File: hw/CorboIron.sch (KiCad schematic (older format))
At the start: 82 parts, among them P1 CONN_01X03, P10 CONN_01X04, P11 CONN_01X04, P2 CONN_01X03, P3 CONN_01X03, P4 DIL32, P5 CONN_01X03, P6 CONN_01X04, P7 CONN_01X02, P8 CONN_01X03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

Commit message: Started PCB
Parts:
- C1, C10, C2, C3, C4, C5, C6, C7: footprint (none) -> Discret:CV3-30PF
- C8, C9: footprint (none) -> Capacitors_SMD:C_1206_HandSoldering
- D1, D3, D4, D5, D7, D9: footprint (none) -> Diodes_SMD:DO-214BA
- D10, D2, D6, D8: footprint (none) -> LEDs:LED_1206
- JP1, JP2: footprint (none) -> Pin_Headers:Pin_Header_Straight_1x02
- P1, P2, P3, P5: footprint (none) -> Connect:bornier3
- P10, P11, P6: footprint (none) -> Pin_Headers:Pin_Header_Straight_1x04
- P4: footprint (none) -> Housings_DIP:DIP-32_W15.24mm_LongPads
- P7: footprint (none) -> Connect:bornier2
- P8, P9: footprint (none) -> Pin_Headers:Pin_Header_Straight_1x03
- Q1, Q2, Q3, Q4: footprint DPAK-5 -> SMD_Packages:DPAK5
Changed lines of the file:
@@
 LIBS:contrib
 LIBS:valves
+LIBS:CorboIron-cache
 EELAYER 25 0
 EELAYER END
@@
 F 0 "P4" H 1650 7750 50  0000 C CNN
 F 1 "DIL32" V 1650 6800 50  0000 C CNN
-F 2 "" H 1650 6800 50  0001 C CNN
+F 2 "Housings_DIP:DIP-32_W15.24mm_LongPads" H 1650 6800 50  0001 C CNN
 F 3 "" H 1650 6800 50  0000 C CNN
 	1    1650 6800
@@
 F 0 "C2" H 1925 3850 50  0000 L CNN
 F 1 "CP1" H 1925 3650 50  0000 L CNN
-F 2 "" H 1900 3750 50  0001 C CNN
+F 2 "Discret:CV3-30PF" H 1900 3750 50  0001 C CNN
 F 3 "" H 1900 3750 50  0000 C CNN
 	1    1900 3750
@@
 F 0 "D3" H 2400 3850 50  0000 C CNN
 F 1 "D" H 2400 3650 50  0000 C CNN
-F 2 "" H 2400 3750 50  0001 C CNN
+F 2 "Diodes_SMD:DO-214BA" H 2400 3750 50  0001 C CNN
 F 3 "" H 2400 3750 50  0000 C CNN
 	1    2400 3750
@@
 F 0 "D4" H 2150 4000 50  0000 C CNN
 F 1 "D" H 2150 3800 50  0000 C CNN
-F 2 "" H 2150 3900 50  0001 C CNN
+F 2 "Diodes_SMD:DO-214BA" H 2150 3900 50  0001 C CNN
 F 3 "" H 2150 3900 50  0000 C CNN
 	1    2150 3900
@@
 F 0 "C3" H 2675 4000 50  0000 L CNN
 F 1 "CP1" H 2675 3800 50  0000 L CNN
-F 2 "" H 2650 3900 50  0001 C CNN
+F 2 "Discret:CV3-30PF" H 2650 3900 50  0001 C CNN
 F 3 "" H 2650 3900 50  0000 C CNN
 	1    2650 3900
@@
 F 0 "Q4" H 13675 8175 50  0000 L CNN
 F 1 "IPS6041RPBF" H 13675 8100 50  0000 L CNN
-F 2 "DPAK-5" H 13675 8025 50  0000 L CNN
+F 2 "SMD_Packages:DPAK5" H 13675 8025 50  0000 L CNN
 F 3 "" H 13350 8100 50  0000 L CNN
 	1    13350 8100
@@
 F 0 "P7" H 3250 9650 50  0000 C CNN
 F 1 "CONN_01X02" V 3350 9500 50  0000 C CNN
-F 2 "" H 3250 9500 50  0001 C CNN
+F 2 "Connect:bornier2" H 3250 9500 50  0001 C CNN
 F 3 "" H 3250 9500 50  0000 C CNN
 	1    3250 9500
@@
 F 0 "C6" H 9125 8400 50  0000 L CNN
 F 1 "CP1" H 9125 8200 50  0000 L CNN
-F 2 "" H 9100 8300 50  0001 C CNN
+F 2 "Discret:CV3-30PF" H 9100 8300 50  0001 C CNN
 F 3 "" H 9100 8300 50  0000 C CNN
 	1    9100 8300
@@
 F 0 "D9" H 8700 8250 50  0000 C CNN
 F 1 "D" H 8700 8050 50  0000 C CNN
-F 2 "" H 8700 8150 50  0001 C CNN
+F 2 "Diodes_SMD:DO-214BA" H 8700 8150 50  0001 C CNN
 F 3 "" H 8700 8150 50  0000 C CNN
 	1    8700 8150
@@
 F 0 "P5" H 14150 8800 50  0000 C CNN
 F 1 "CONN_01X03" V 14250 8600 50  0000 C CNN
-F 2 "" H 14150 8600 50  0001 C CNN
+F 2 "Connect:bornier3" H 14150 8600 50  0001 C CNN
 F 3 "" H 14150 8600 50  0000 C CNN
 	1    14150 8600
@@
 F 0 "D10" H 10950 8600 50  0000 C CNN
 F 1 "LED" H 10950 8400 50  0000 C CNN
-F 2 "" H 10950 8500 50  0001 C CNN
+F 2 "LEDs:LED_1206" H 10950 8500 50  0001 C CNN
 F 3 "" H 10950 8500 50  0000 C CNN
 	1    10950 8500
@@
 F 0 "P6" H 1900 8900 50  0000 C CNN
 F 1 "CONN_01X04" V 2000 8650 50  0000 C CNN
-F 2 "" H 1900 8650 50  0001 C CNN
+F 2 "Pin_Headers:Pin_Header_Straight_1x04" H 1900 8650 50  0001 C CNN
 F 3 "" H 1900 8650 50  0000 C CNN
 	1    1900 8650
@@
 F 0 "Q3" H 13675 6275 50  0000 L CNN
 F 1 "IPS6041RPBF" H 13675 6200 50  0000 L CNN
-F 2 "DPAK-5" H 13675 6125 50  0000 L CNN
+F 2 "SMD_Packages:DPAK5" H 13675 6125 50  0000 L CNN
 F 3 "" H 13350 6200 50  0000 L CNN
 	1    13350 6200
@@
 F 0 "C5" H 9125 6500 50  0000 L CNN
 F 1 "CP1" H 9125 6300 50  0000 L CNN
-F 2 "" H 9100 6400 50  0001 C CNN
+F 2 "Discret:CV3-30PF" H 9100 6400 50  0001 C CNN
 F 3 "" H 9100 6400 50  0000 C CNN
 	1    9100 6400
@@
 F 0 "D7" H 8700 6350 50  0000 C CNN
 F 1 "D" H 8700 6150 50  0000 C CNN
-F 2 "" H 8700 6250 50  0001 C CNN
+F 2 "Diodes_SMD:DO-214BA" H 8700 6250 50  0001 C CNN
 F 3 "" H 8700 6250 50  0000 C CNN
 	1    8700 6250
@@
 F 0 "P3" H 14150 6900 50  0000 C CNN
 F 1 "CONN_01X03" V 14250 6700 50  0000 C CNN
-F 2 "" H 14150 6700 50  0001 C CNN
+F 2 "Connect:bornier3" H 14150 6700 50  0001 C CNN
 F 3 "" H 14150 6700 50  0000 C CNN
 	1    14150 6700
@@
 F 0 "D8" H 10950 6700 50  0000 C CNN
 F 1 "LED" H 10950 6500 50  0000 C CNN
-F 2 "" H 10950 6600 50  0001 C CNN
+F 2 "LEDs:LED_1206" H 10950 6600 50  0001 C CNN
 F 3 "" H 10950 6600 50  0000 C CNN
 	1    10950 6600
@@
 F 0 "Q2" H 13675 4275 50  0000 L CNN
 F 1 "IPS6041RPBF" H 13675 4200 50  0000 L CNN
-F 2 "DPAK-5" H 13675 4125 50  0000 L CNN
+F 2 "SMD_Packages:DPAK5" H 13675 4125 50  0000 L CNN
 F 3 "" H 13350 4200 50  0000 L CNN
 	1    13350 4200
@@
 F 0 "C4" H 9125 4500 50  0000 L CNN
 F 1 "CP1" H 9125 4300 50  0000 L CNN
-F 2 "" H 9100 4400 50  0001 C CNN
+F 2 "Discret:CV3-30PF" H 9100 4400 50  0001 C CNN
 F 3 "" H 9100 4400 50  0000 C CNN
 	1    9100 4400
@@
 F 0 "D5" H 8700 4350 50  0000 C CNN
 F 1 "D" H 8700 4150 50  0000 C CNN
-F 2 "" H 8700 4250 50  0001 C CNN
+F 2 "Diodes_SMD:DO-214BA" H 8700 4250 50  0001 C CNN
 F 3 "" H 8700 4250 50  0000 C CNN
 	1    8700 4250
@@
 F 0 "P2" H 14150 4900 50  0000 C CNN
 F 1 "CONN_01X03" V 14250 4700 50  0000 C CNN
-F 2 "" H 14150 4700 50  0001 C CNN
+F 2 "Connect:bornier3" H 14150 4700 50  0001 C CNN
 F 3 "" H 14150 4700 50  0000 C CNN
 	1    14150 4700
@@
 F 0 "D6" H 10950 4700 50  0000 C CNN
 F 1 "LED" H 10950 4500 50  0000 C CNN
-F 2 "" H 10950 4600 50  0001 C CNN
+F 2 "LEDs:LED_1206" H 10950 4600 50  0001 C CNN
 F 3 "" H 10950 4600 50  0000 C CNN
 	1    10950 4600
@@
 F 0 "Q1" H 13675 2375 50  0000 L CNN
 F 1 "IPS6041RPBF" H 13675 2300 50  0000 L CNN
-F 2 "DPAK-5" H 13675 2225 50  0000 L CNN
+F 2 "SMD_Packages:DPAK5" H 13675 2225 50  0000 L CNN
 F 3 "" H 13350 2300 50  0000 L CNN
 	1    13350 2300
@@
 F 0 "C1" H 9125 2600 50  0000 L CNN
 F 1 "CP1" H 9125 2400 50  0000 L CNN
-F 2 "" H 9100 2500 50  0001 C CNN
+F 2 "Discret:CV3-30PF" H 9100 2500 50  0001 C CNN
 F 3 "" H 9100 2500 50  0000 C CNN
 	1    9100 2500
@@
 F 0 "D1" H 8700 2450 50  0000 C CNN
 F 1 "D" H 8700 2250 50  0000 C CNN
-F 2 "" H 8700 2350 50  0001 C CNN
+F 2 "Diodes_SMD:DO-214BA" H 8700 2350 50  0001 C CNN
 F 3 "" H 8700 2350 50  0000 C CNN
 	1    8700 2350
@@
 F 0 "P1" H 14150 3000 50  0000 C CNN
 F 1 "CONN_01X03" V 14250 2800 50  0000 C CNN
-F 2 "" H 14150 2800 50  0001 C CNN
+F 2 "Connect:bornier3" H 14150 2800 50  0001 C CNN
 F 3 "" H 14150 2800 50  0000 C CNN
 	1    14150 2800
@@
 F 0 "D2" H 10950 2800 50  0000 C CNN
 F 1 "LED" H 10950 2600 50  0000 C CNN
-F 2 "" H 10950 2700 50  0001 C CNN
+F 2 "LEDs:LED_1206" H 10950 2700 50  0001 C CNN
 F 3 "" H 10950 2700 50  0000 C CNN
 	1    10950 2700
@@
 F 0 "P10" H 4450 8600 50  0000 C CNN
 F 1 "CONN_01X04" V 4550 8350 50  0000 C CNN
-F 2 "" H 4450 8350 50  0001 C CNN
+F 2 "Pin_Headers:Pin_Header_Straight_1x04" H 4450 8350 50  0001 C CNN
 F 3 "" H 4450 8350 50  0000 C CNN
 	1    4450 8350
@@
 F 0 "P11" H 2850 9050 50  0000 C CNN
 F 1 "CONN_01X04" V 2950 8800 50  0000 C CNN
-F 2 "" H 2850 8800 50  0001 C CNN
+F 2 "Pin_Headers:Pin_Header_Straight_1x04" H 2850 8800 50  0001 C CNN
 F 3 "" H 2850 8800 50  0000 C CNN
 	1    2850 8800
@@
 F 0 "P8" H 4500 7550 50  0000 C CNN
 F 1 "CONN_01X03" V 4600 7350 50  0000 C CNN
-F 2 "" H 4500 7350 50  0001 C CNN
+F 2 "Pin_Headers:Pin_Header_Straight_1x03" H 4500 7350 50  0001 C CNN
 F 3 "" H 4500 7350 50  0000 C CNN
 	1    4500 7350
@@
 F 0 "P9" H 5350 7550 50  0000 C CNN
 F 1 "CONN_01X03" V 5450 7350 50  0000 C CNN
-F 2 "" H 5350 7350 50  0001 C CNN
+F 2 "Pin_Headers:Pin_Header_Straight_1x03" H 5350 7350 50  0001 C CNN
 F 3 "" H 5350 7350 50  0000 C CNN
 	1    5350 7350
@@
 F 0 "C10" H 6175 10450 50  0000 L CNN
 F 1 "CP1" H 6175 10250 50  0000 L CNN
-F 2 "" H 6150 10350 50  0001 C CNN
+F 2 "Discret:CV3-30PF" H 6150 10350 50  0001 C CNN
 F 3 "" H 6150 10350 50  0000 C CNN
 	1    6150 10350
@@
 F 0 "C9" H 5925 10450 50  0000 L CNN
 F 1 "C" H 5925 10250 50  0000 L CNN
-F 2 "" H 5938 10200 50  0001 C CNN
+F 2 "Capacitors_SMD:C_1206_HandSoldering" H 5938 10200 50  0001 C CNN
 F 3 "" H 5900 10350 50  0000 C CNN
 	1    5900 10350
@@
 F 0 "C8" H 4925 10450 50  0000 L CNN
 F 1 "C" H 4925 10250 50  0000 L CNN
-F 2 "" H 4938 10200 50  0001 C CNN
+F 2 "Capacitors_SMD:C_1206_HandSoldering" H 4938 10200 50  0001 C CNN
 F 3 "" H 4900 10350 50  0000 C CNN
 	1    4900 10350
@@
 F 0 "C7" H 4675 10450 50  0000 L CNN
 F 1 "CP1" H 4675 10250 50  0000 L CNN
-F 2 "" H 4650 10350 50  0001 C CNN
+F 2 "Discret:CV3-30PF" H 4650 10350 50  0001 C CNN
 F 3 "" H 4650 10350 50  0000 C CNN
 	1    4650 10350
@@
 F 0 "JP1" H 6100 10030 50  0000 C CNN
 F 1 "Jumper_NO_Small" H 6110 9890 50  0001 C CNN
-F 2 "" H 6100 9950 50  0001 C CNN
+F 2 "Pin_Headers:Pin_Header_Straight_1x02" H 6100 9950 50  0001 C CNN
 F 3 "" H 6100 9950 50  0000 C CNN
 	1    6100 9950
@@
 F 0 "JP2" H 1000 8080 50  0000 C CNN
 F 1 "Jumper_NO_Small" H 1010 7940 50  0001 C CNN
-F 2 "" H 1000 8000 50  0001 C CNN
+F 2 "Pin_Headers:Pin_Header_Straight_1x02" H 1000 8000 50  0001 C CNN
 F 3 "" H 1000 8000 50  0000 C CNN
 	1    1000 8000

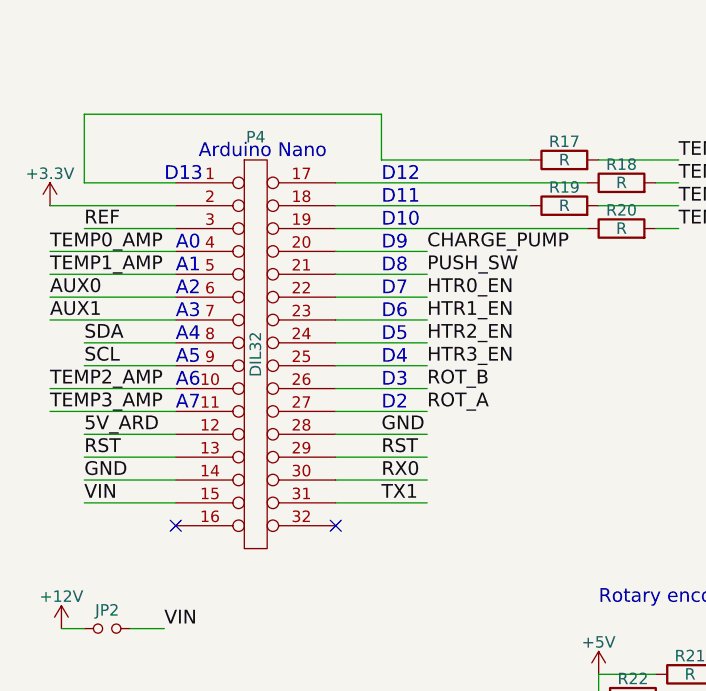
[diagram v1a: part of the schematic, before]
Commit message: Started placing componets
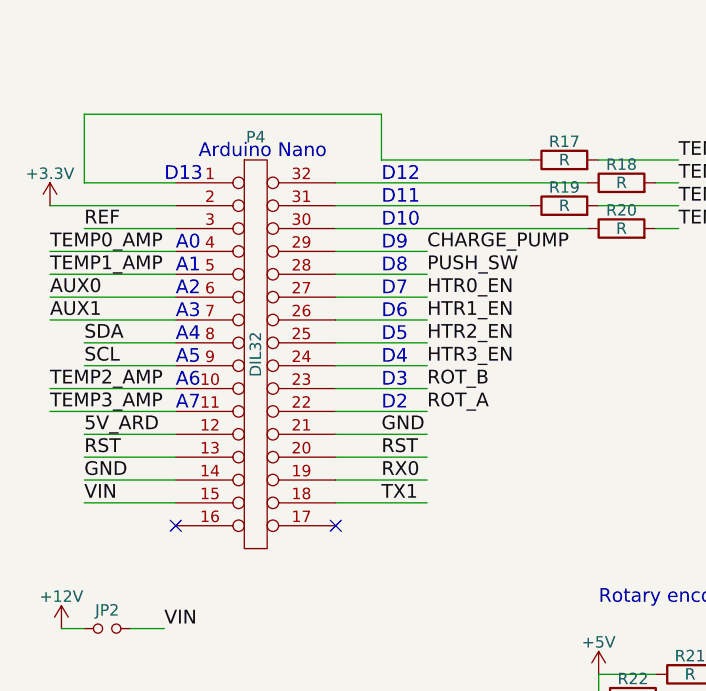
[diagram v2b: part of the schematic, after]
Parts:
- removed P4: DIL32, Housings_DIP:DIP-32_W15.24mm_LongPads, symbol DIL32
- added P4: DIL32, symbol DIL32-RESCUE-CorboIron
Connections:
- net +3V3: now also P4.2 (P2)
- net 5V_ARD: now also P4.12 (P12)
- net AUX0: now also P4.6 (P6)
- net AUX1: now also P4.7 (P7)
- net CHARGE_PUMP: now also P4.29 (P29)
- net GND: now also P4.14 (P14), P4.21 (P21)
- net HTR0_EN: now also P4.27 (P27)
- net HTR1_EN: now also P4.26 (P26)
- net HTR2_EN: now also P4.25 (P25)
- net HTR3_EN: now also P4.24 (P24)
- net PUSH_SW: now also P4.28 (P28)
- net REF: now also P4.3 (P3)
- net ROT_A: now also P4.22 (P22)
- net ROT_B: now also P4.23 (P23)
- net RST: now also P4.13 (P13), P4.20 (P20)
- net RX0: now also P4.19 (P19)
- net SCL: now also P4.9 (P9)
- net SDA: now also P4.8 (P8)
- net TEMP0_AMP: now also P4.4 (P4)
- net TEMP1_AMP: now also P4.5 (P5)
- net TEMP2_AMP: now also P4.10 (P10)
- net TEMP3_AMP: now also P4.11 (P11)
- net TX1: now also P4.18 (P18)
- net VIN: now also P4.15 (P15)
- net at R17.1: now also P4.1 (P1)
- net at R18.1: now also P4.32 (P32)
- net at R19.1: now also P4.31 (P31)
- net at R20.1: now also P4.30 (P30)
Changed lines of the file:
@@
 EESchema Schematic File Version 2
+LIBS:CorboIron-rescue
 LIBS:power
 LIBS:device
@@
 Comment4 ""
 $EndDescr
-$Comp
-L DIL32 P4
-U 1 1 56ED3F0B
-P 1650 6800
-F 0 "P4" H 1650 7750 50  0000 C CNN
-F 1 "DIL32" V 1650 6800 50  0000 C CNN
-F 2 "Housings_DIP:DIP-32_W15.24mm_LongPads" H 1650 6800 50  0001 C CNN
-F 3 "" H 1650 6800 50  0000 C CNN
-	1    1650 6800
-	1    0    0    -1
-$EndComp
 Text Label 900  6250 0    60   ~ 0
 REF
@@
 Wire Wire Line
 	1250 8000 1100 8000
+$Comp
+L DIL32-RESCUE-CorboIron P4
+U 1 1 56EF51CE
+P 1650 6800
+F 0 "P4" H 1650 7750 50  0000 C CNN
+F 1 "DIL32" V 1650 6800 50  0000 C CNN
+F 2 "" H 1650 6800 50  0000 C CNN
+F 3 "" H 1650 6800 50  0000 C CNN
+	1    1650 6800
+	1    0    0    -1
+$EndComp
 $EndSCHEMATC

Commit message: Horror!
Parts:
- removed P4: DIL32, symbol DIL32-RESCUE-CorboIron
- added P4: Arduino_nano, symbol Arduino_nano
- U14: symbol 7805 -> 7805-RESCUE-CorboIron
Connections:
- net +12V: now also U14.1 (VI); no longer U14.VI
- net +3V3: now also P4.2 (P2)
- net +5V: now also U14.3 (VO); no longer U14.VO
- net 5V_ARD: now also P4.12 (P12)
- net AUX0: now also P4.6 (P6)
- net AUX1: now also P4.7 (P7)
- net CHARGE_PUMP: now also P4.29 (P29)
- net GND: now also U14.2 (GND), P4.14 (P14), P4.21 (P21); no longer U14.GND
- net HTR0_EN: now also P4.27 (P27)
- net HTR1_EN: now also P4.26 (P26)
- net HTR2_EN: now also P4.25 (P25)
- net HTR3_EN: now also P4.24 (P24)
- net PUSH_SW: now also P4.28 (P28)
- net REF: now also P4.3 (P3)
- net ROT_A: now also P4.22 (P22)
- net ROT_B: now also P4.23 (P23)
- net RX0: now also P4.19 (P19)
- net SCL: now also P4.9 (P9)
- net SDA: now also P4.8 (P8)
- net TEMP0_AMP: now also P4.4 (P4)
- net TEMP0_MIN: no longer C4.1, D5.2 (A), R5.1, U6.2 (-), U7.2 (-)
- net TEMP1_AMP: now also P4.5 (P5)
- net TEMP2_AMP: now also P4.10 (P10)
- net TEMP3_AMP: now also P4.11 (P11)
- net TX1: now also P4.18 (P18)
- net VIN: now also P4.15 (P15)
- net V_NEG: now also RV2.2, RV4.2, RV6.2, U2.4 (V-), U5.4 (V-), U8.4 (V-)
- net at R20.1: now also P4.30 (P30)
- net at R19.1: now also P4.31 (P31)
- net at R18.1: now also P4.32 (P32)
- net at R17.1: now also P4.1 (P1)
- new net TEMP2_MIN: C4.1, D5.2 (A), R5.1, U6.2 (-), U7.2 (-)
- no-connect marks 18 -> 20
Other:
- note added: "Add fan control!!!!"
- note added: "RST"
